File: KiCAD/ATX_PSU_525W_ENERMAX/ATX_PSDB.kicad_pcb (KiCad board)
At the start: 2 copper layers, 87 parts, among them J1 Fan1, J10 EPS12V 8 Pin, J11 Current Sens, J12 Molex: 0039281243, J13 Molex: 0039281243, J14 Molex: 0039281243, J15 Potti, J16 Potti, J17 LED Yellow, J18 LED Yellow, J19 Volt Sens, J2 Power On Switch, J20 12V Out, J21 Volt Sens, J22 12V Out, J23 Molex: 0039281243, J24 Current Sens, J25 Current Sens, J26 Molex: 0039281243, J27 Molex: 0039281243, J28 Fan1, J29 Fan1, J3 Standby LED, J30 Potti, J31 Potti, J32 LED Red, J33 LED Orange, J34 Volt Sens, J35 5V Out, J36 Volt Sens, J37 3.3V Out, J38 Screw_Terminal_01x06, J39 Screw_Terminal_01x06, J4 EPS12V 4Pin, J40 Current Sens, J41 Current Sens, J42 Screw_Terminal_01x06, J43 Screw_Terminal_01x06, J44 Screw_Terminal_01x12, J5 Potti, J6 LED Yellow, J7 Volt Sens, J8 12V Out, J9 Main ATX 24Pin, Q1 Q_NMOS_DGS, Q2 Q_NMOS_DGS, Q3 Q_NMOS_DGS, Q4 Q_NMOS_DGS, Q5 Q_NMOS_DGS, U1 ACS712xLCTR-20A, U2 ACS712xLCTR-20A, U3 ACS712xLCTR-20A, U4 ACS712xLCTR-20A, U5 ACS712xLCTR-20A

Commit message: changed terminal blocks to wago footprints
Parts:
- J10: footprint Connector_Molex:Molex_Mini-Fit_Jr_5566-12A_2x06_P4.20mm_Vertical -> Connector_Molex:Molex_Mini-Fit_Jr_5566-08A_2x04_P4.20mm_Vertical
- J20, J22, J35, J37, J8: footprint TerminalBlock_Altech:Altech_AK300_1x02_P5.00mm_45-Degree -> TerminalBlock_WAGO:TerminalBlock_WAGO_236-102_1x02_P5.00mm_45Degree
- J38, J39, J42, J43: footprint TerminalBlock_RND:TerminalBlock_RND_205-00005_1x06_P5.00mm_Horizontal -> TerminalBlock_WAGO:TerminalBlock_WAGO_236-108_1x08_P5.00mm_45Degree
- J44: footprint TerminalBlock_RND:TerminalBlock_RND_205-00011_1x12_P5.00mm_Horizontal -> TerminalBlock_WAGO:TerminalBlock_WAGO_236-112_1x12_P5.00mm_45Degree
- R7: footprint Resistor_THT:R_Axial_Power_L20.0mm_W6.4mm_P25.40mm -> Resistor_THT:R_Axial_DIN0516_L15.5mm_D5.0mm_P20.32mm_Horizontal
- moved R5 133.2 mm to (99.1, 82.5), turned to 270 degrees
- moved DZ3 114.9 mm to (111.8, 135.9), turned to 270 degrees
- moved R7 88.5 mm to (101.6, 130.8), turned to 270 degrees
- moved J44 59.6 mm to (95.2, 165.1), turned to 180 degrees
- moved F1 58.5 mm to (88.9, 17.8), turned to 270 degrees
- moved F2 51.1 mm to (86.4, 71.1), turned to 270 degrees
- moved J38 49.8 mm to (58.4, 43.2)
- moved J27 36.8 mm to (16.5, 143.5)
- moved J23 35.6 mm to (16.5, 128.3)
- moved J26 34.3 mm to (16.5, 113.0)
- moved J4 34.3 mm to (16.5, 16.5), turned to 0 degrees
- moved J39 33.6 mm to (58.4, 102.9)
- moved J14 33.0 mm to (16.5, 82.5)
- moved J12 31.8 mm to (16.5, 67.3)
- moved J13 30.0 mm to (16.5, 52.1)
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
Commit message: More pcb layout
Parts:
- moved J2 300.1 mm to (17.8, 27.9), turned to 90 degrees
- moved J3 275.1 mm to (17.8, 38.1), turned to 90 degrees
- moved R4 212.9 mm to (17.8, 63.5), turned to 90 degrees
- moved DZ5 187.6 mm to (137.2, 19.1), turned to 270 degrees
- moved J43 171.1 mm to (47.0, 17.8)
- moved DZ4 165.2 mm to (137.2, 43.2), turned to 270 degrees
- moved J15 157.8 mm to (158.8, 119.4), turned to 270 degrees
- moved R11 155.0 mm to (143.5, 15.2)
- moved J17 148.8 mm to (137.2, 123.2), turned to 90 degrees
- moved Q5 148.4 mm to (234.9, 20.3)
- moved J9 147.0 mm to (35.6, 16.5), turned to 270 degrees
- moved J41 145.1 mm to (223.5, 19.1)
- moved J36 140.9 mm to (266.7, 17.8)
- moved DZ2 140.8 mm to (137.2, 110.5), turned to 270 degrees
- moved J42 139.1 mm to (47.0, 41.9)
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
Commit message: More pcb layout
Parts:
- moved J32 129.7 mm to (138.4, 47.0), turned to 180 degrees
- moved J36 127.3 mm to (139.7, 8.89), turned to 180 degrees
- moved J29 117.4 mm to (163.8, -3.81), turned to 270 degrees
- moved J31 98.1 mm to (179.1, 10.2), turned to 90 degrees
- moved J18 89.0 mm to (138.4, 161.3), turned to 180 degrees
- moved J40 88.4 mm to (153.7, 21.6), turned to 180 degrees
- moved J28 71.2 mm to (161.3, 36.8), turned to 270 degrees
- moved J25 67.6 mm to (170.2, 146.1), turned to 90 degrees
- moved Q3 67.3 mm to (171.4, 152.4), turned to 270 degrees
- moved J8 66.0 mm to (171.4, 69.8)
- moved J16 58.6 mm to (161.3, 162.6), turned to 90 degrees
- moved C9 58.6 mm to (160.0, 24.1), turned to 270 degrees
- moved C7 58.0 mm to (162.6, 24.1), turned to 270 degrees
- moved Q4 56.6 mm to (171.4, 39.4), turned to 270 degrees
- moved J22 53.4 mm to (207.0, 146.1), turned to 270 degrees
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
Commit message: More pcb layout
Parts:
- J10: value EPS12V 8 Pin -> ATX12V1 8 Pin
- J13: value Molex: 0039281243 -> 12V2
- J4: value EPS12V 4Pin -> ATX12V1
- R1, R10, R11, R12, R3, R5, R6, R7, R8, R9: footprint Resistor_THT:R_Axial_DIN0516_L15.5mm_D5.0mm_P20.32mm_Horizontal -> Resistor_SMD:R_2816_7142Metric_Pad3.20x4.45mm_HandSolder
- moved J21 43.9 mm to (179.3, 134.6), turned to 180 degrees
- moved J1 32.8 mm to (152.4, 59.7), turned to 0 degrees
- moved J16 28.9 mm to (153.9, 134.6), turned to 180 degrees
- moved J18 26.8 mm to (141.2, 134.6)
- moved J22 26.5 mm to (180.8, 150.4), turned to 180 degrees
- moved HS1 26.3 mm to (200.4, 140.5)
- moved Q3 25.2 mm to (192.0, 137.9)
- moved DZ3 18.9 mm to (124.0, 135.1), turned to 180 degrees
- moved J5 17.8 mm to (171.4, 87.6), turned to 0 degrees
- moved J11 17.7 mm to (170.2, 66.0), turned to 270 degrees
- moved J8 16.2 mm to (160.0, 81.3)
- moved R8 15.3 mm to (151.4, 147.3), turned to 270 degrees
- moved C1 12.5 mm to (163.8, 63.5), turned to 180 degrees
- moved J25 12.3 mm to (165.6, 134.6), turned to 180 degrees
- moved C2 12.2 mm to (159.6, 63.5), turned to 180 degrees
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
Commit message: densified circuit, defined edge cut, added mounting holes
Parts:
- added REF**: OSHW-Logo, Symbol:OSHW-Logo2_14.6x12mm_Copper, F.Cu at (196.6, 55.9)
- added REF**: MountingHole_4.3mm_M4_Pad_Via, MountingHole:MountingHole_4.3mm_M4_Pad_Via, F.Cu at (224.0, 213.9)
- added REF**: MountingHole_4.3mm_M4_Pad_Via, MountingHole:MountingHole_4.3mm_M4_Pad_Via, F.Cu at (75.7, 213.9)
- added REF**: MountingHole_4.3mm_M4_Pad_Via, MountingHole:MountingHole_4.3mm_M4_Pad_Via, F.Cu at (75.7, 55.9)
- added REF**: MountingHole_4.3mm_M4_Pad_Via, MountingHole:MountingHole_4.3mm_M4_Pad_Via, F.Cu at (222.5, 56.9)
- R4: footprint Resistor_THT:R_Axial_DIN0516_L15.5mm_D5.0mm_P20.32mm_Horizontal -> Resistor_SMD:R_2816_7142Metric_Pad3.20x4.45mm_HandSolder
- moved J3 130.5 mm to (112.3, 128.1), turned to 0 degrees
- moved J33 128.2 mm to (176.8, 66.0), turned to 180 degrees
- moved R4 122.7 mm to (121.9, 128.5), turned to 0 degrees
- moved J43 105.6 mm to (121.4, 71.1), turned to 180 degrees
- moved R11 98.6 mm to (186.4, 80.3), turned to 90 degrees
- moved J9 95.8 mm to (105.2, 82.3)
- moved F5 91.8 mm to (130.0, 80.0)
- moved J2 91.1 mm to (90.9, 82.3)
- moved J36 90.4 mm to (209.8, 66.0), turned to 0 degrees
- moved J42 88.6 mm to (119.9, 83.3), turned to 270 degrees
- moved U4 88.4 mm to (197.9, 111.0)
- moved C7 88.4 mm to (199.1, 104.6)
- moved C9 88.4 mm to (196.6, 104.6)
- moved J40 87.5 mm to (200.4, 95.5)
- moved R9 87.1 mm to (174.8, 109.7), turned to 90 degrees
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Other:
- board outline added: 160 x 170 mm
- board text added: "ATX Power Supply Distribution Board V. 1.0"

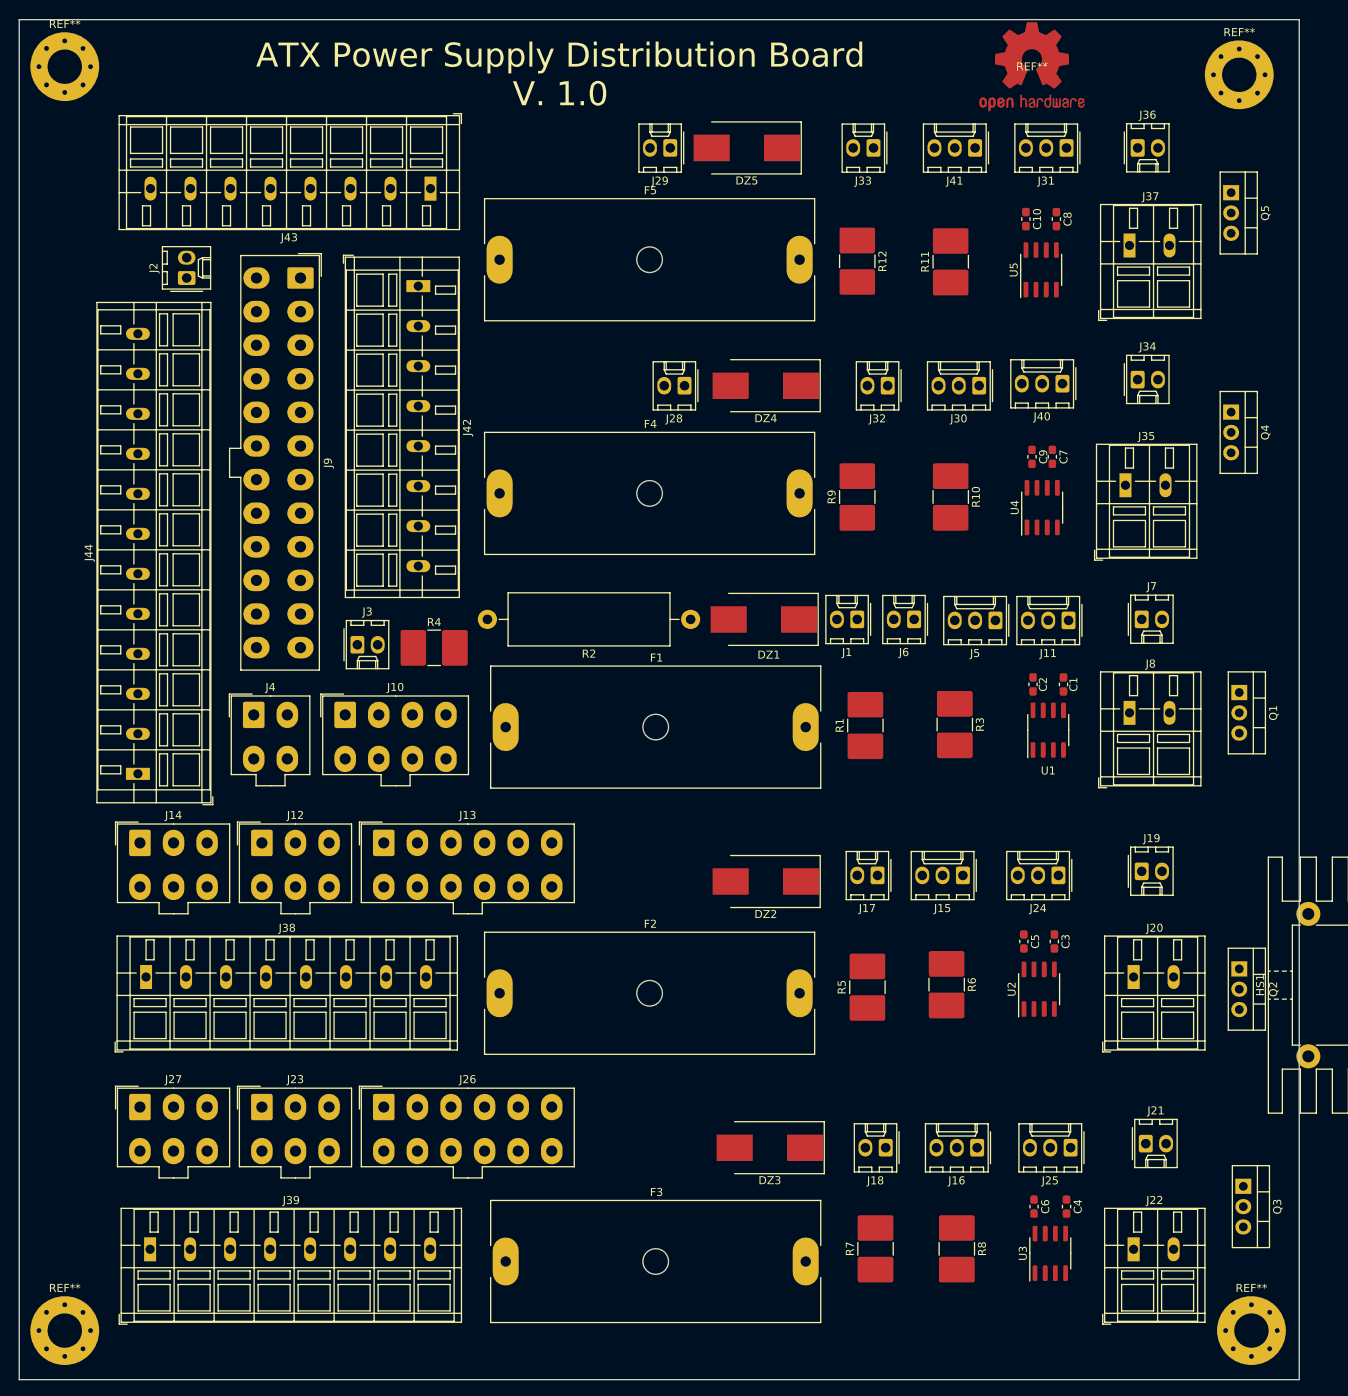
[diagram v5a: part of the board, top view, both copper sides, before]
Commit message: Adding Traces
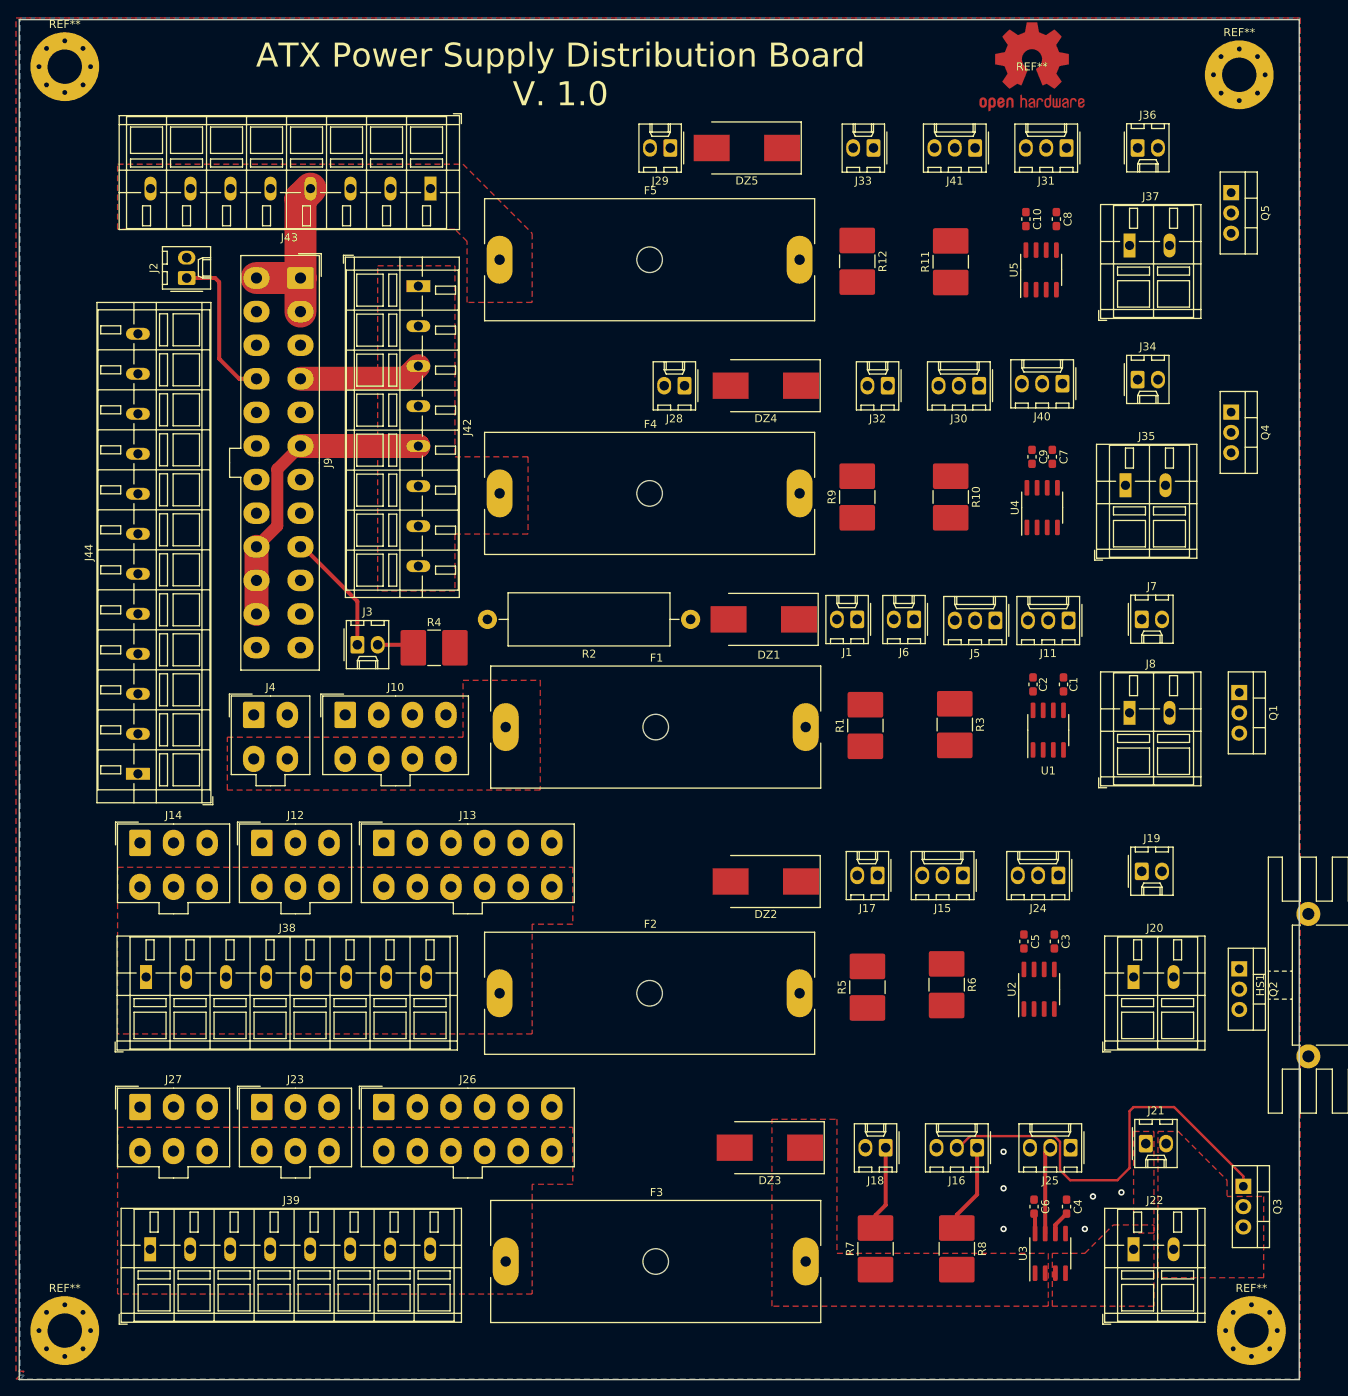
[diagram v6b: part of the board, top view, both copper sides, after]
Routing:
- net +5V: track 0.00 -> 56.2 mm
- net Net-(J16-Pad2): track 0.00 -> 53.9 mm
- net +3.3V: track 0.00 -> 21.4 mm
- net PS_ON: track 0.00 -> 19.6 mm
- net +5VSB: track 0.00 -> 15.4 mm
- net Net-(J16-Pad1): track 0.00 -> 12.2 mm
- net Net-(J25-Pad2): track 0.00 -> 11.0 mm
- net Net-(J18-Pad1): track 0.00 -> 10.6 mm
- net Net-(J3-Pad2): track 0.00 -> 4.61 mm
- net Net-(C4-Pad2): track 0.00 -> 3.07 mm
- net GND: vias 0 -> 6
- added copper zone on F.Cu, net +12V1
- added copper zone on F.Cu, net +12V2
- added copper zone on F.Cu, net +12V3
- added copper zone on F.Cu, net +3.3V
- added copper zone on F.Cu, net +5V
- added copper zone on F.Cu, net 12V3-
- added copper zone on B.Cu, net GND
- added copper zone on F.Cu, net GND
- added copper zone on F.Cu, net Net-(DZ3-Pad1)
- added copper zone on F.Cu, net Net-(J21-Pad1)

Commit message: More traces
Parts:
- moved J28 20.1 mm to (173.2, 95.5), turned to 0 degrees
- moved J29 19.3 mm to (170.7, 66.0), turned to 0 degrees
- moved R12 14.2 mm to (189.0, 80.3)
- moved J41 11.2 mm to (200.7, 66.0)
- moved J31 9.40 mm to (191.5, 66.0)
- moved R11 7.62 mm to (178.8, 80.3)
- moved J33 5.59 mm to (182.4, 66.0)
- moved REF** 5.59 mm to (202.2, 55.9)
- moved J32 4.33 mm to (182.9, 95.5)
- moved J30 2.05 mm to (192.0, 95.5)
- moved J1 2.03 mm to (172.7, 125.0), turned to 0 degrees
- moved J6 1.02 mm to (182.9, 125.0)
- moved J40 0.76 mm to (201.2, 95.5)
- moved C7 0.51 mm to (199.6, 104.6)
- moved C9 0.51 mm to (196.1, 104.6)
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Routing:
- net Net-(J15-Pad2): track 0.00 -> 52.5 mm
- net Net-(J5-Pad2): track 0.00 -> 47.1 mm
- net Net-(J31-Pad2): track 0.00 -> 40.4 mm
- net Net-(J30-Pad2): track 0.00 -> 39.5 mm
- net Net-(J32-Pad1): track 0.00 -> 17.3 mm
- net Net-(J6-Pad1): track 0.00 -> 15.7 mm
- net Net-(J30-Pad1): track 0.00 -> 13.9 mm
- net Net-(J40-Pad2): track 0.00 -> 13.6 mm
- net Net-(J41-Pad2): track 0.00 -> 13.2 mm
- net Net-(J33-Pad1): track 0.00 -> 13.1 mm
- net Net-(J31-Pad1): track 0.00 -> 12.7 mm
- net Net-(J5-Pad1): track 0.00 -> 12.5 mm
- net Net-(J24-Pad2): track 0.00 -> 12.0 mm
- net Net-(J15-Pad1): track 0.00 -> 11.9 mm
- net Net-(J17-Pad1): track 0.00 -> 11.9 mm
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- added copper zone on F.Cu, net 12V1-
- added copper zone on F.Cu, net 12V2-
- added copper zone on F.Cu, net 3.3V-
- added copper zone on F.Cu, net 5V-
- added copper zone on F.Cu, net Net-(DZ1-Pad1)
- added copper zone on F.Cu, net Net-(DZ2-Pad1)
- added copper zone on F.Cu, net Net-(DZ4-Pad1)
- added copper zone on F.Cu, net Net-(DZ5-Pad1)
- added copper zone on F.Cu, net Net-(J19-Pad1)
- added copper zone on F.Cu, net Net-(J34-Pad1)
- added copper zone on F.Cu, net Net-(J36-Pad1)
- added copper zone on F.Cu, net Net-(J7-Pad1)

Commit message: more traces
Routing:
- net +5V: track 67.4 -> 345.8 mm
- net +12V1: track 0.00 -> 37.0 mm
- net +3.3V: track 21.4 -> 57.5 mm
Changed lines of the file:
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@@
     (thickness 1.6)
     (drawings 5)
-    (tracks 115)
+    (tracks 143)
     (zones 0)
     (modules 92)
@@
   )
   (setup
-    (last_trace_width 0.5)
+    (last_trace_width 2)
     (user_trace_width 0.3)
     (user_trace_width 0.5)
@@
   (segment (start 195.961 108.523) (end 195.961 105.65) (width 0.5) (layer F.Cu) (net 3))
   (segment (start 195.834 78.805) (end 195.834 75.805) (width 0.5) (layer F.Cu) (net 3))
+  (segment (start 200.66 94.996) (end 201.168 95.504) (width 1) (layer B.Cu) (net 3))
+  (segment (start 200.66 66.04) (end 200.66 94.996) (width 1) (layer B.Cu) (net 3))
+  (segment (start 201.168 96.604) (end 201.168 125.095) (width 1) (layer B.Cu) (net 3))
+  (segment (start 200.768 156.972) (end 199.898 156.972) (width 1) (layer B.Cu) (net 3))
+  (segment (start 201.168 156.572) (end 200.768 156.972) (width 1) (layer B.Cu) (net 3))
+  (segment (start 201.168 125.095) (end 201.168 156.572) (width 1) (layer B.Cu) (net 3))
+  (segment (start 199.898 189.484) (end 201.422 191.008) (width 1) (layer B.Cu) (net 3))
+  (segment (start 199.898 156.972) (end 199.898 189.484) (width 1) (layer B.Cu) (net 3))
+  (segment (start 201.168 123.995) (end 201.168 125.095) (width 1.5) (layer B.Cu) (net 3))
+  (segment (start 146.770999 122.817999) (end 199.990999 122.817999) (width 1.5) (layer B.Cu) (net 3))
+  (segment (start 133.173 109.22) (end 146.770999 122.817999) (width 1.5) (layer B.Cu) (net 3))
+  (segment (start 199.990999 122.817999) (end 201.168 123.995) (width 1.5) (layer B.Cu) (net 3))
+  (segment (start 201.168 96.604) (end 201.168 95.504) (width 1.5) (layer B.Cu) (net 3))
+  (segment (start 200.21799 97.55401) (end 201.168 96.604) (width 1.5) (layer B.Cu) (net 3))
+  (segment (start 133.173 109.22) (end 144.83899 97.55401) (width 1.5) (layer B.Cu) (net 3))
+  (segment (start 144.83899 97.55401) (end 200.21799 97.55401) (width 1.5) (layer B.Cu) (net 3))
+  (segment (start 130.048 109.22) (end 133.173 109.22) (width 1.5) (layer B.Cu) (net 3))
   (segment (start 198.12 167.372) (end 199.39 166.102) (width 0.5) (layer F.Cu) (net 4))
   (segment (start 198.12 168.721) (end 198.12 167.372) (width 0.5) (layer F.Cu) (net 4))
@@
   (segment (start 198.374 77.075) (end 199.644 75.805) (width 0.5) (layer F.Cu) (net 7))
   (segment (start 198.374 78.805) (end 198.374 77.075) (width 0.5) (layer F.Cu) (net 7))
+  (segment (start 105.156 120.096) (end 105.156 124.296) (width 3) (layer F.Cu) (net 13))
+  (segment (start 125.93599 133.55599) (end 130.81 138.43) (width 3) (layer F.Cu) (net 13))
+  (segment (start 112.651722 133.55599) (end 125.93599 133.55599) (width 3) (layer F.Cu) (net 13))
+  (segment (start 109.69799 130.602258) (end 112.651722 133.55599) (width 3) (layer F.Cu) (net 13))
+  (segment (start 109.69799 128.424625) (end 109.69799 130.602258) (width 3) (layer F.Cu) (net 13))
+  (segment (start 105.569365 124.296) (end 109.69799 128.424625) (width 3) (layer F.Cu) (net 13))
+  (segment (start 105.156 124.296) (end 105.569365 124.296) (width 3) (layer F.Cu) (net 13))
   (segment (start 105.156 86.496) (end 105.156 82.296) (width 4) (layer F.Cu) (net 16))
-  (segment (start 105.156 72.376) (end 106.412 71.12) (width 4) (layer F.Cu) (net 16))
-  (segment (start 105.156 82.296) (end 105.156 72.376) (width 4) (layer F.Cu) (net 16))
   (segment (start 99.656 82.296) (end 105.156 82.296) (width 4) (layer F.Cu) (net 16))
+  (segment (start 98.299752 131.04601) (end 88.36201 121.108268) (width 2) (layer F.Cu) (net 16))
+  (segment (start 102.30599 131.04601) (end 98.299752 131.04601) (width 2) (layer F.Cu) (net 16))
+  (segment (start 104.856 128.496) (end 102.30599 131.04601) (width 2) (layer F.Cu) (net 16))
+  (segment (start 105.156 128.496) (end 104.856 128.496) (width 2) (layer F.Cu) (net 16))
+  (segment (start 107.442 80.01) (end 130.048 80.01) (width 4) (layer F.Cu) (net 16))
+  (segment (start 105.156 82.296) (end 107.442 80.01) (width 4) (layer F.Cu) (net 16))
   (segment (start 97.506 94.896) (end 94.996 92.386) (width 0.5) (layer F.Cu) (net 17))
   (segment (start 99.656 94.896) (end 97.506 94.896) (width 0.5) (layer F.Cu) (net 17))
